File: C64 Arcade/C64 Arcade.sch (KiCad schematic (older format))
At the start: 48 parts, among them J1 Port_1, J10 P2_FIRE3, J11 P1_FIRE1, J12 P1_FIRE2, J13 P1_FIRE3, J14 EXT_PWR, J2 Port_2, J3 DIRECTION, J4 UP, J5 RIGHT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

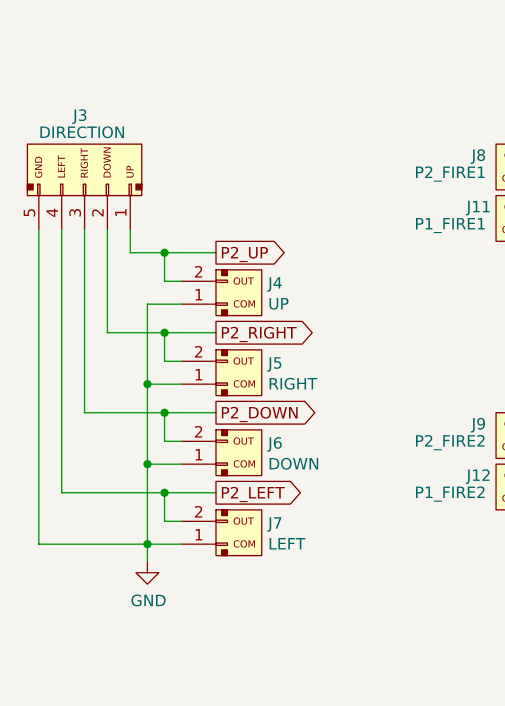
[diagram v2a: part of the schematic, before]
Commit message: Added UP_EN for direction
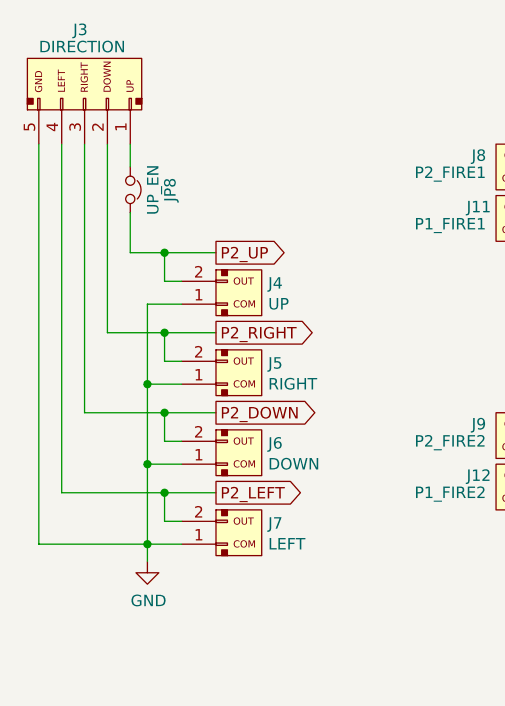
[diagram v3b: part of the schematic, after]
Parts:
- added JP8: UP_EN, Connector_PinHeader_2.54mm:PinHeader_1x02_P2.54mm_Vertical, symbol Device:Jumper_NC_Small
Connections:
- net P2_UP: now also JP8.2; no longer J3.1 (Pin_1)
- new net: J3.1 (Pin_1), JP8.1
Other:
- moved on the sheet: J3
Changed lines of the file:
@@
 L arcade:DIR J3
 U 1 1 601F1F84
-P 1000 1225
-F 0 "J3" V 1300 1275 50  0000 R CNN
-F 1 "DIRECTION" V 1225 1425 50  0000 R CNN
-F 2 "Connector_JST:JST_XH_B5B-XH-A_1x05_P2.50mm_Vertical" H 1000 1225 50  0001 C CNN
-F 3 "~" H 1000 1225 50  0001 C CNN
-	1    1000 1225
+P 1000 850
+F 0 "J3" V 1300 900 50  0000 R CNN
+F 1 "DIRECTION" V 1225 1050 50  0000 R CNN
+F 2 "Connector_JST:JST_XH_B5B-XH-A_1x05_P2.50mm_Vertical" H 1000 850 50  0001 C CNN
+F 3 "~" H 1000 850 50  0001 C CNN
+	1    1000 850
 	0    -1   -1   0
 $EndComp
@@
 Connection ~ 1350 1525
 Wire Wire Line
-	1200 1425 1200 1525
-Wire Wire Line
 	1200 1525 1350 1525
 Wire Wire Line
-	1100 1425 1100 1875
-Wire Wire Line
 	1100 1875 1350 1875
 Wire Wire Line
-	1000 1425 1000 2225
-Wire Wire Line
 	1000 2225 1350 2225
 Wire Wire Line
-	900  1425 900  2575
-Wire Wire Line
 	900  2575 1350 2575
-Wire Wire Line
-	800  1425 800  2800
 Wire Wire Line
 	800  2800 1275 2800
@@
 	8900 1400 10250 1400
 Connection ~ 8900 1400
+$Comp
+L Device:Jumper_NC_Small JP8
+U 1 1 601D8F08
+P 1200 1250
+F 0 "JP8" H 1200 1425 50  0000 C CNN
+F 1 "UP_EN" H 1200 1350 50  0000 C CNN
+F 2 "Connector_PinHeader_2.54mm:PinHeader_1x02_P2.54mm_Vertical" H 1200 1250 50  0001 C CNN
+F 3 "~" H 1200 1250 50  0001 C CNN
+	1    1200 1250
+	0    1    1    0
+$EndComp
+Wire Wire Line
+	1200 1350 1200 1525
+Wire Wire Line
+	1200 1150 1200 1050
+Wire Wire Line
+	1100 1050 1100 1875
+Wire Wire Line
+	1000 1050 1000 2225
+Wire Wire Line
+	900  1050 900  2575
+Wire Wire Line
+	800  1050 800  2800
 $EndSCHEMATC

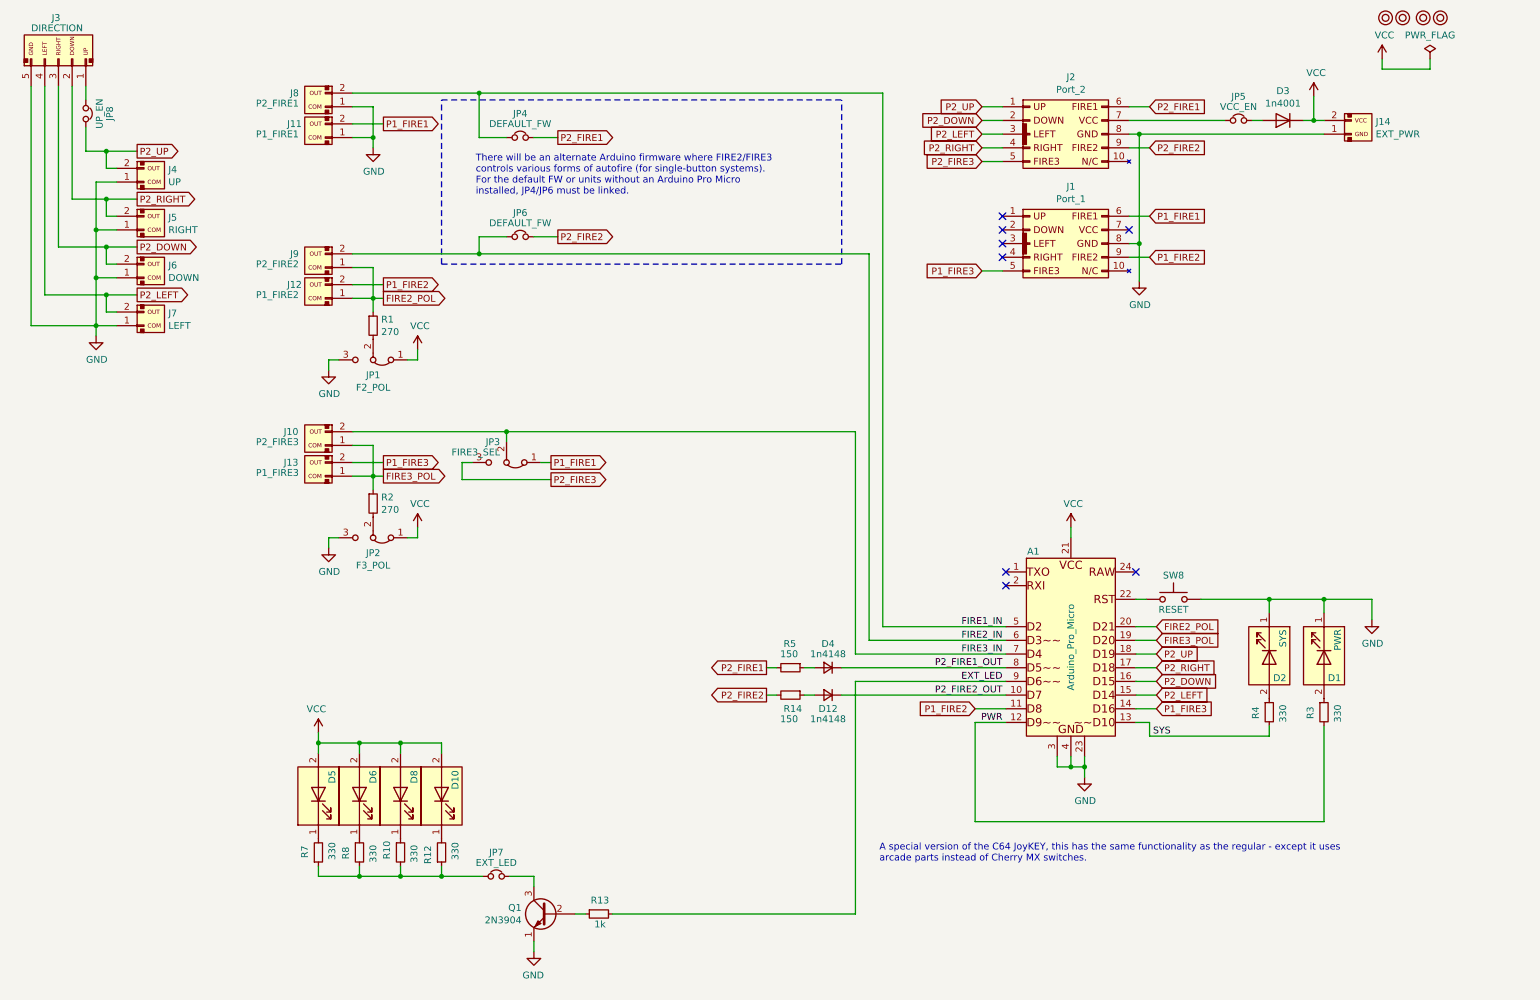
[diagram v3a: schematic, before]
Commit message: Fixed Arcade pinout and added isolation for Arduino (need new layout)
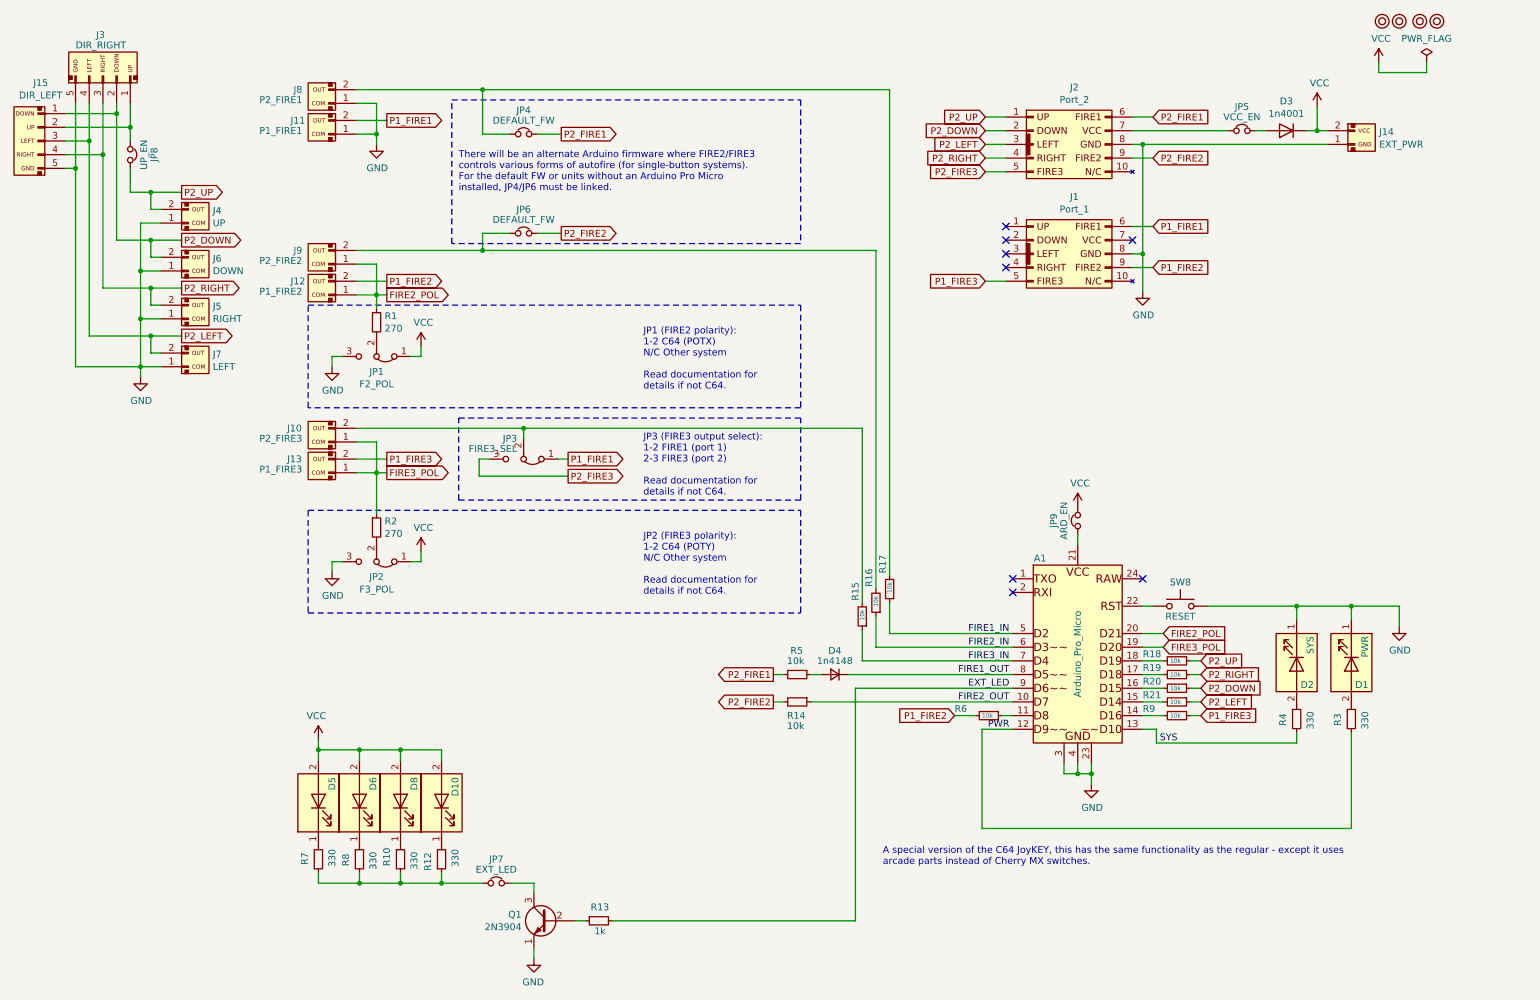
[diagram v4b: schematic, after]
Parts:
- removed D12: 1n4148, Diode_THT:D_DO-35_SOD27_P7.62mm_Horizontal, symbol Device:D_Small
- added J15: DIR_LEFT, symbol arcade:DIR_REV
- added JP9: ARD_EN, Connector_PinHeader_2.54mm:PinHeader_1x02_P2.54mm_Vertical, symbol Device:Jumper_NC_Small
- added R15, R16, R17, R18, R19, R20, R21, R6, R9: 10k, Resistor_THT:R_Axial_DIN0207_L6.3mm_D2.5mm_P10.16mm_Horizontal, symbol Device:R_Small
- J3: value DIRECTION -> DIR_RIGHT
- R14, R5: value 150 -> 10k
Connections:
- net P2_FIRE2_OUT is gone; now on net FIRE2_OUT: A1.10 (D7)
- net FIRE1_IN: now also R17.1; no longer J8.2 (Pin_2), JP4.1
- net FIRE2_IN: now also R16.1; no longer J9.2 (Pin_2), JP6.1
- net FIRE3_IN: now also R15.1; no longer J10.2 (Pin_2), JP3.2 (C)
- net GND: now also J15.5 (Pin_5)
- net P1_FIRE2: now also R6.2; no longer A1.11 (D8)
- net P1_FIRE3: now also R9.1; no longer A1.14 (D16)
- net P2_DOWN: now also J3.2 (Pin_2), J15.1 (Pin_1), R20.1; no longer A1.16 (D15), J3.3 (Pin_3)
- net P2_LEFT: now also J15.3 (Pin_3), R21.1; no longer A1.15 (D14)
- net P2_RIGHT: now also J3.3 (Pin_3), J15.4 (Pin_4), R19.1; no longer A1.17 (D18), J3.2 (Pin_2)
- net P2_UP: now also R18.1; no longer A1.18 (D19)
- net VCC: now also JP9.2; no longer A1.21 (VCC)
- net FIRE2_OUT: now reaches R14.1
- net at J3.1 (Pin_1), JP8.1: now also J15.2 (Pin_2)
- net P2_FIRE1_OUT renamed FIRE1_OUT
- new net: J9.2 (Pin_2), JP6.1, R16.2
- new net: J8.2 (Pin_2), JP4.1, R17.2
- new net: A1.21 (VCC), JP9.1
- new net: A1.15 (D14), R21.2
- new net: J10.2 (Pin_2), JP3.2 (C), R15.2
- new net: A1.14 (D16), R9.2
- new net: A1.11 (D8), R6.1
- new net: A1.16 (D15), R20.2
- new net: A1.17 (D18), R19.2
- new net: A1.18 (D19), R18.2
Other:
- note added: "JP1 (FIRE2 polarity):\n1-2 C64 (POTX)\nN/C Other system\n\nRead documentation for\ndetails if not C64."
- note added: "JP2 (FIRE3 polarity):\n1-2 C64 (POTY)\nN/C Other system\n\nRead documentation for\ndetails if not C64.\n"
- note added: "JP3 (FIRE3 output select):\n1-2 FIRE1 (port 1)\n2-3 FIRE3 (port 2)\n\nRead documentation for\ndetails if not C64."
- moved on the sheet: D1, D10, D2, D5, D6, D8, J10, J11, J12, J13, J14, J3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
